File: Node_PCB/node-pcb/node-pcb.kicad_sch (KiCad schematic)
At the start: 56 parts, among them J1 TYPE-C-31-M-12, J2 BM08B-GHS-TBT(LF)(SN), J3 BM08B-GHS-TBT(LF)(SN), J4 TC2030, J5 AFC11-S12ICA-00, Q1 S8050, SW1 TS-1187A-B-A-B, U1 NCP1117ST33T3G, U2 W25Q32JVSSIQ, U3 RP2040, U4 THVD1450DR, Y1 ABM8-272-T3

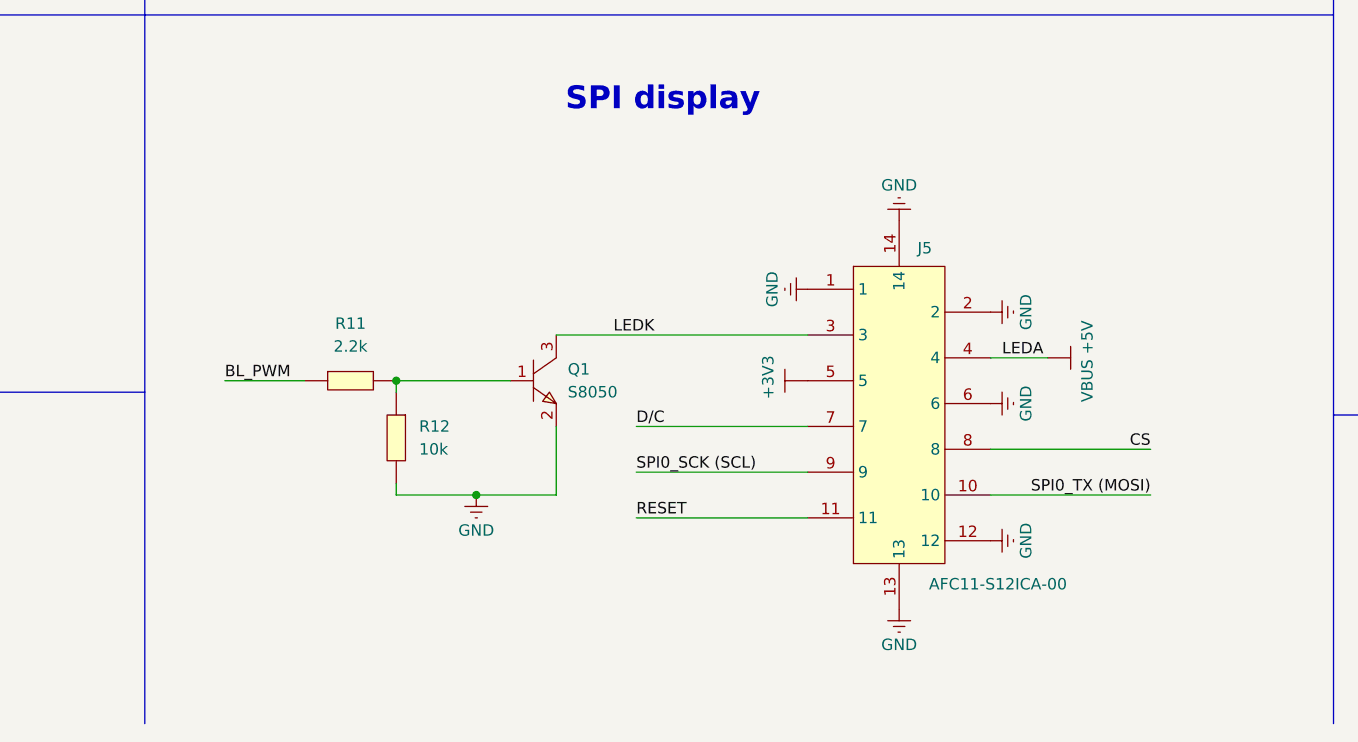
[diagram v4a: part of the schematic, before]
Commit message: Update schematic and documentation
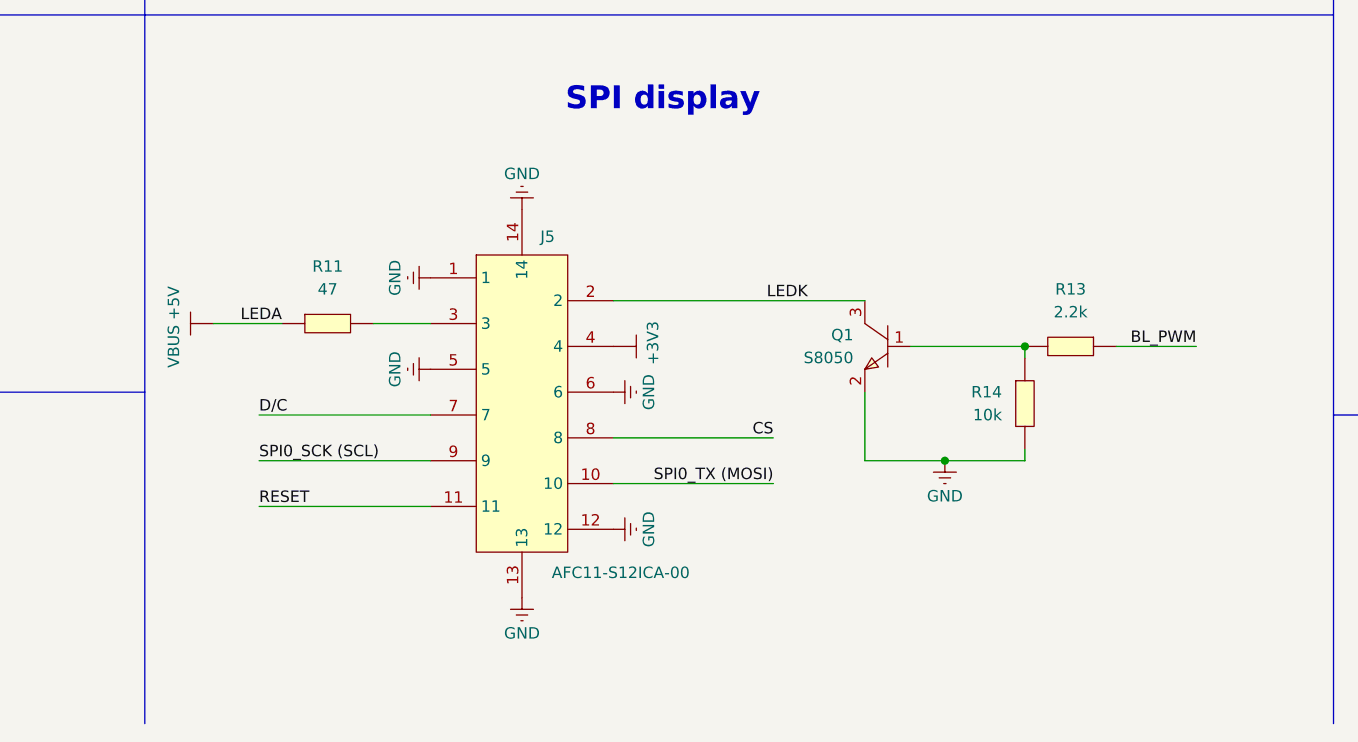
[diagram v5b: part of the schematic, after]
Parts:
- removed R11: 2.2k, EasyEDA:R0402, symbol EasyEDA:0402WGF2201TCE
- removed R12: 10k, EasyEDA:R0402, symbol EasyEDA:0402WGF1002TCE
- added R11: 47, EasyEDA:R0805, symbol JLC_Import:0805W8F470JT5E
- added R13: 2.2k, EasyEDA:R0402, symbol EasyEDA:0402WGF2201TCE
- added R14: 10k, EasyEDA:R0402, symbol EasyEDA:0402WGF1002TCE
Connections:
- net +3V3: now also J5.4; no longer J5.5
- net BL_PWM: now also R13.1
- net GND: now also J5.5, R14.2; no longer J5.2
- net LEDK: now also J5.2; no longer J5.3
- net VBUS +5V: now also R11.1; no longer J5.4
- net at Q1.1 (B): now also R13.2, R14.1
- new net: J5.3, R11.2
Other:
- moved on the sheet: J5
